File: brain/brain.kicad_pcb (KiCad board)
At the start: 2 copper layers, 48.5 x 56 mm, 7 parts, among them J0 BAR0, J1 BAR1, J2 I2C, J5 XTRA, SW1 RESET, U1 Elite-C

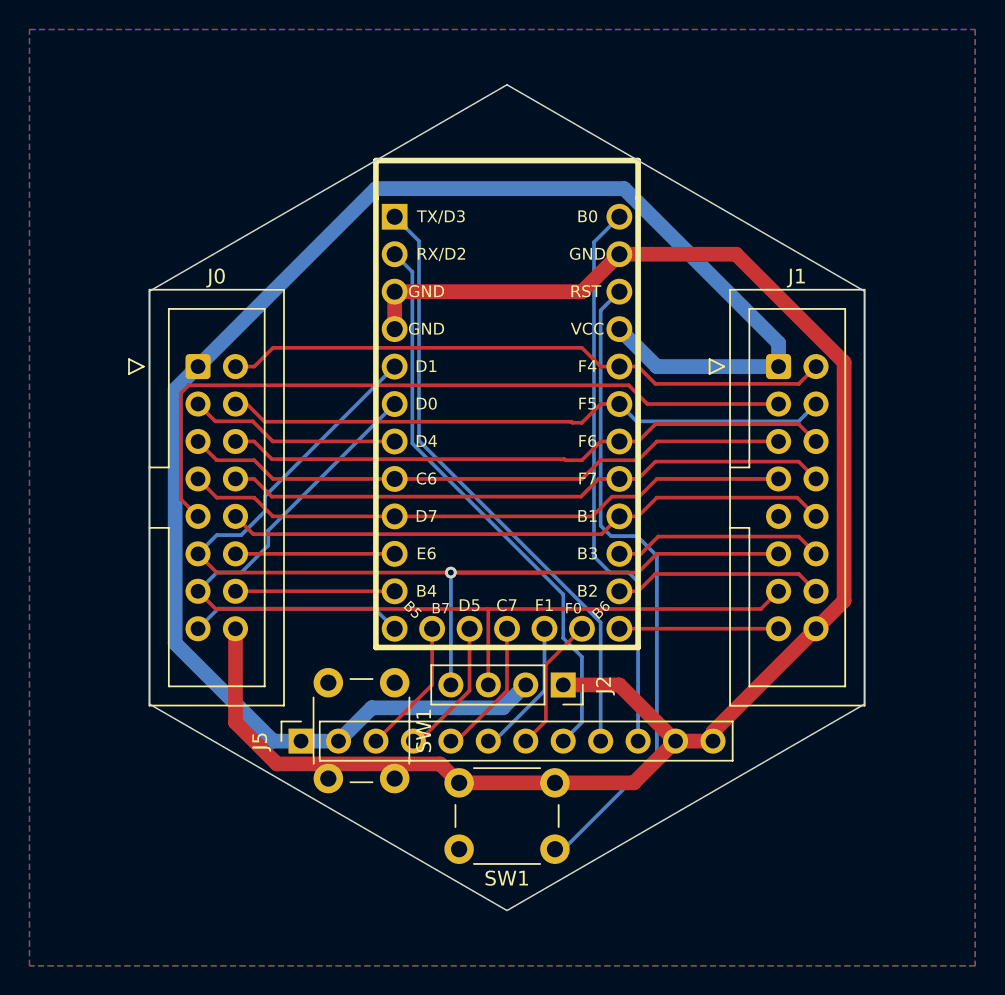
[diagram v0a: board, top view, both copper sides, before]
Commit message: Use interrupt-enabled pins for encoder0 and int1
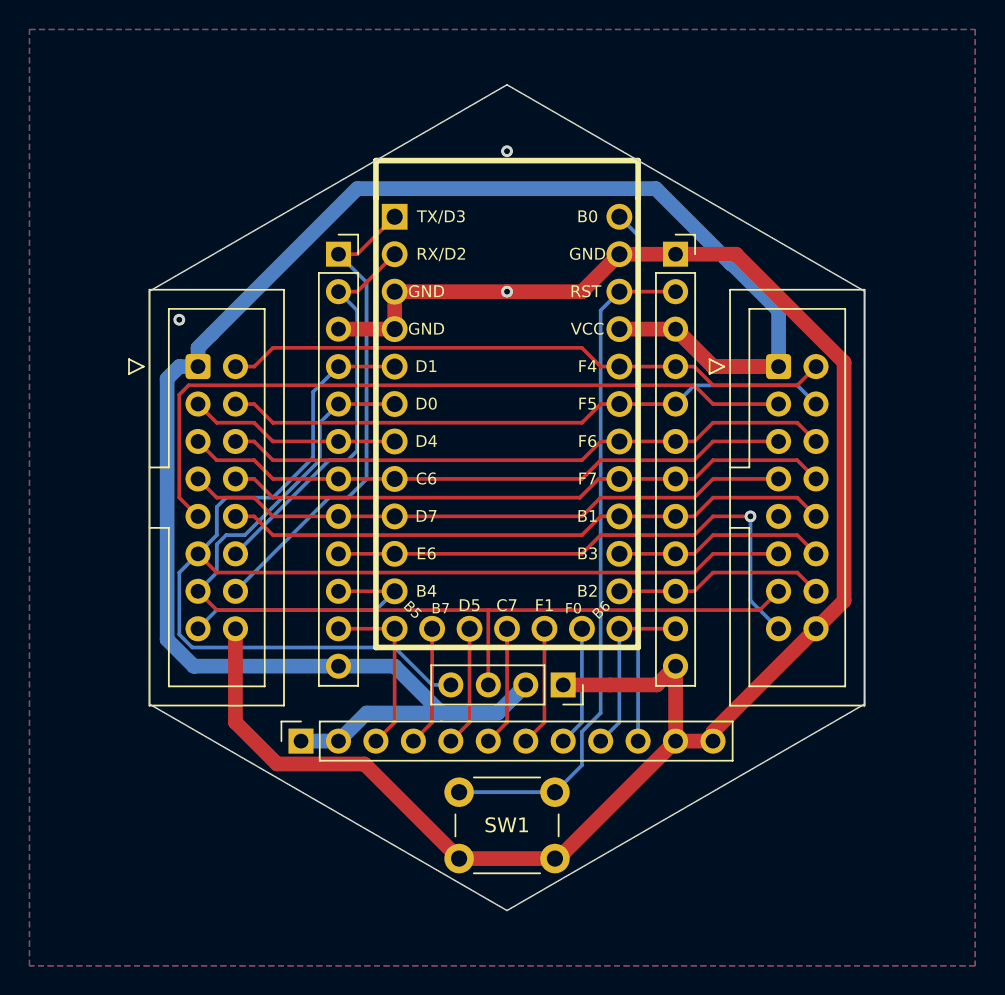
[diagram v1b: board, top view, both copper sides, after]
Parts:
- removed the SW1 at (170.2, 114.2)
- added J3: SIDE0, Connector_PinSocket_2.54mm:PinSocket_1x12_P2.54mm_Vertical, F.Cu at (166.4, 85.1)
- added J4: SIDE1, Connector_PinSocket_2.54mm:PinSocket_1x12_P2.54mm_Vertical, F.Cu at (189.2, 85.1)
- moved SW1 7.56 mm to (174.6, 121.6), turned to 0 degrees
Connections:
- J5 pad 3: /B7 -> /B5
- J5 pad 4: /D5 -> /B7
- J5 pad 5: /C7 -> /D5
- J5 pad 6: /F1 -> /C7
- J5 pad 7: /F0 -> /F1
- J5 pad 8: /RX -> /F0
- J5 pad 9: /TX -> /B6
- U1 pad 1: /TX -> /ENC0_B
- U1 pad 10: /ENC0_A -> /INT1
- U1 pad 11: /ENC0_B -> /INT0
- U1 pad 12: /INT0 -> /B5
- U1 pad 13: /INT1 -> /B6
- U1 pad 2: /RX -> /ENC0_A
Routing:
- net /TX: track 41.3 -> 0.00 mm
- net /RX: track 38.8 -> 0.00 mm
- net /INT1: track 10.8 -> 37.4 mm, vias 0 -> 1
- net VCC: track 109.7 -> 134.3 mm
- net /ENC0_B: track 10.8 -> 32.9 mm
- net /ENC0_A: track 10.8 -> 27.3 mm
- net /SDA: track 73.6 -> 88.6 mm, vias 1 -> 0
- net /B5: track 0.00 -> 12.0 mm
- net /B6: track 0.00 -> 12.0 mm
- net GND: track 117.3 -> 129.2 mm, vias 0 -> 3
- net /INT0: track 14.5 -> 18.2 mm
- net /RB0: track 38.3 -> 36.1 mm
- net /SCL: track 64.7 -> 66.7 mm
- net /RST: track 44.4 -> 46.1 mm
- net /F0: track 9.20 -> 8.14 mm
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- added copper zone on B.Cu, net GND
- removed copper zone on B.Cu, net VCC

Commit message: Brain: Add mounting holes and silkscreen labels
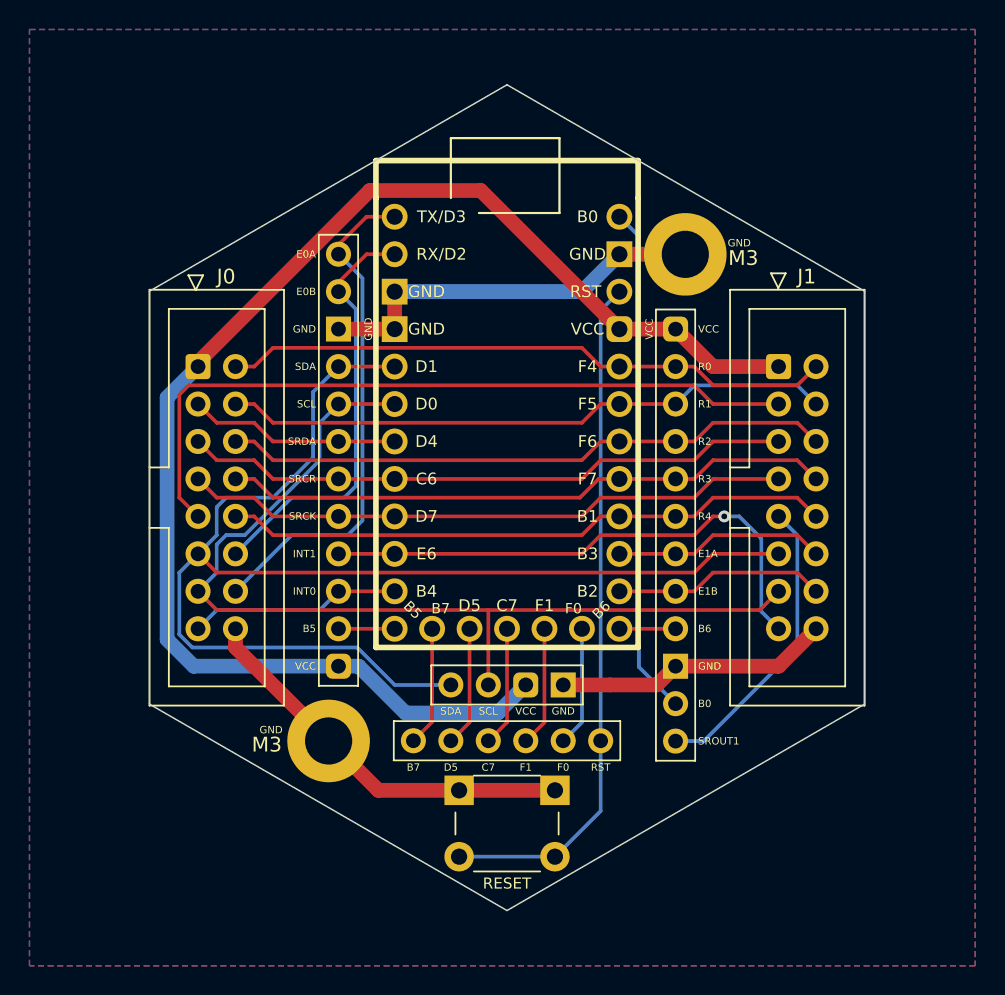
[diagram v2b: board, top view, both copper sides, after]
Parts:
- added H1: M3, MountingHole:MountingHole_3.2mm_M3_DIN965_Pad, F.Cu at (189.9, 85.1)
- added H2: M3, MountingHole:MountingHole_3.2mm_M3_DIN965_Pad, F.Cu at (165.7, 118.1)
- J5: footprint Connector_PinSocket_2.54mm:PinSocket_1x12_P2.54mm_Vertical -> Connector_PinSocket_2.54mm:PinSocket_1x06_P2.54mm_Vertical
- moved SW1 7.83 mm to (181.1, 125.9), turned to 180 degrees
- moved J5 7.62 mm to (171.4, 118.1)
- moved J4 5.08 mm to (189.2, 90.2)
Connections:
- J4 pad 1: GND -> VCC
- J4 pad 10: /ENC1_B -> GND
- J4 pad 11: /B6 -> /RB0
- J4 pad 12: GND -> /SROUT1
- J4 pad 2: /RST -> /ROW0
- J4 pad 3: VCC -> /ROW1
- J4 pad 4: /ROW0 -> /ROW2
- J4 pad 5: /ROW1 -> /ROW3
- J4 pad 6: /ROW2 -> /ROW4
- J4 pad 7: /ROW3 -> /ENC1_A
- J4 pad 8: /ROW4 -> /ENC1_B
- J4 pad 9: /ENC1_A -> /B6
- J5 pad 1: VCC -> /B7
- J5 pad 2: VCC -> /D5
- J5 pad 3: /B5 -> /C7
- J5 pad 4: /B7 -> /F1
- J5 pad 5: /D5 -> /F0
- J5 pad 6: /C7 -> /RST
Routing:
- net GND: track 129.2 -> 72.8 mm, vias 3 -> 0
- net VCC: track 134.3 -> 96.0 mm
- net /SROUT1: track 0.00 -> 20.3 mm
- net /B5: track 12.0 -> 3.81 mm
- net /B6: track 12.0 -> 3.81 mm
- net /INT0: track 18.2 -> 14.4 mm
- net /ENC0_A: track 27.3 -> 29.0 mm
- net /ENC0_B: track 32.9 -> 34.6 mm
- net /RB0: track 36.1 -> 34.6 mm
- net /RST: track 46.1 -> 46.6 mm
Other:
- board text added: "B0"
- board text added: "B5"
- board text added: "B6"
- board text added: "B7"
- board text added: "C7"
- board text added: "D5"
- board text added: "E0A"
- board text added: "E0B"
- board text added: "E1A"
- board text added: "E1B"
- board text added: "F0"
- board text added: "F1"
- board text added: "GND"
- board text added: "INT0"
- board text added: "INT1"
- board text added: "R0"
- board text added: "R1"
- board text added: "R2"
- board text added: "R3"
- board text added: "R4"
- board text added: "RESET"
- board text added: "RST"
- board text added: "SCL"
- board text added: "SDA"
- board text added: "SQUEEZEBRAIN v1"
- board text added: "SR CLK"
- board text added: "SR CLR"
- board text added: "SR DA"
- board text added: "SR OUT 0"
- board text added: "SR OUT 1"
- board text added: "SRCK"
- board text added: "SRCLK"
- board text added: "SRCLR"
- board text added: "SRCR"
- board text added: "SRDA"
- board text added: "SROUT1"
- board text added: "VCC"
- board text added: "github.com/encukou/squeezebar"

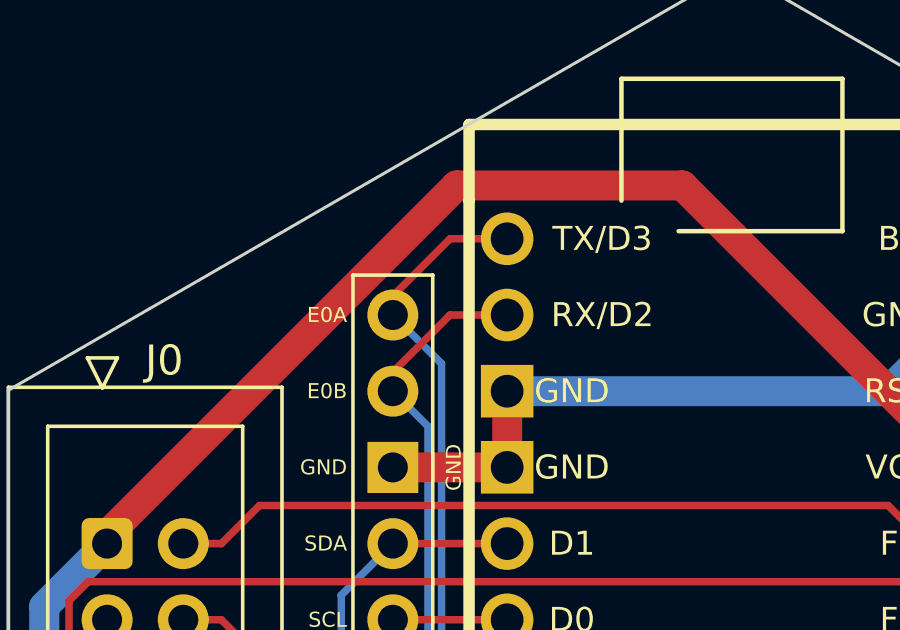
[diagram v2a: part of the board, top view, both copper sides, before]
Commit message: Add SqueezeBarrel
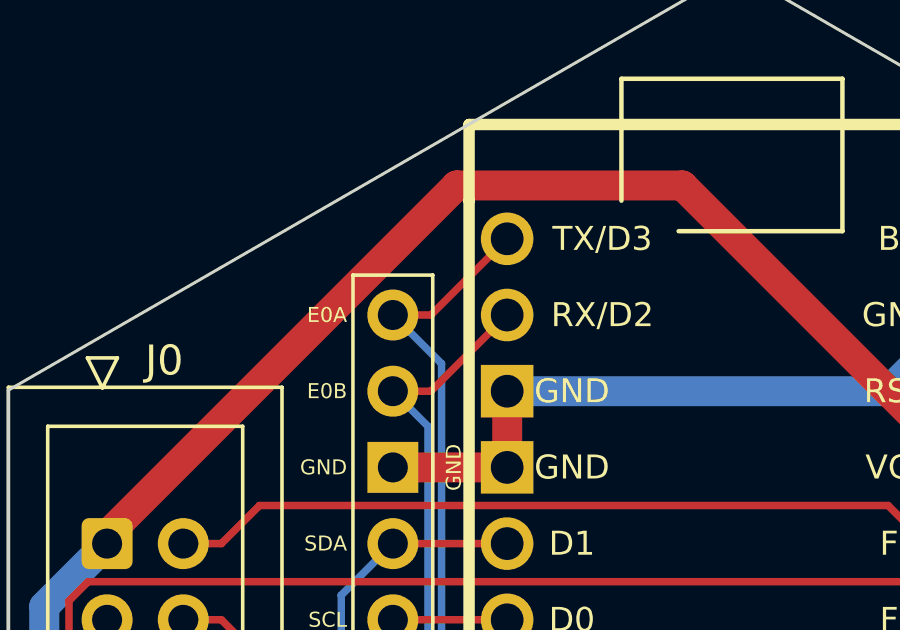
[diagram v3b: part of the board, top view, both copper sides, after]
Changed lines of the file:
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@@
   (segment (start 156.21 93.98) (end 190.5 93.98) (width 0.25) (layer "F.Cu") (net 13))
   (segment (start 155.575 94.615) (end 156.21 93.98) (width 0.25) (layer "F.Cu") (net 13))
-  (segment (start 168.275 85.09) (end 170.18 85.09) (width 0.25) (layer "F.Cu") (net 14))
-  (segment (start 166.37 87.63) (end 166.37 86.995) (width 0.25) (layer "F.Cu") (net 14))
-  (segment (start 166.37 86.995) (end 168.275 85.09) (width 0.25) (layer "F.Cu") (net 14))
+  (segment (start 167.64 87.63) (end 170.18 85.09) (width 0.25) (layer "F.Cu") (net 14))
+  (segment (start 166.37 87.63) (end 167.64 87.63) (width 0.25) (layer "F.Cu") (net 14))
   (segment (start 166.761701 101.6) (end 167.545 100.816701) (width 0.25) (layer "B.Cu") (net 14))
   (segment (start 167.545 88.805) (end 166.37 87.63) (width 0.25) (layer "B.Cu") (net 14))
@@
   (segment (start 167.545 100.816701) (end 167.545 88.805) (width 0.25) (layer "B.Cu") (net 14))
   (segment (start 163.196396 101.6) (end 166.761701 101.6) (width 0.25) (layer "B.Cu") (net 14))
-  (segment (start 166.37 85.09) (end 166.37 84.455) (width 0.25) (layer "F.Cu") (net 15))
-  (segment (start 166.37 84.455) (end 168.275 82.55) (width 0.25) (layer "F.Cu") (net 15))
-  (segment (start 168.275 82.55) (end 170.18 82.55) (width 0.25) (layer "F.Cu") (net 15))
+  (segment (start 170.18 82.55) (end 167.64 85.09) (width 0.25) (layer "F.Cu") (net 15))
+  (segment (start 167.64 85.09) (end 166.37 85.09) (width 0.25) (layer "F.Cu") (net 15))
   (segment (start 167.005 104.14) (end 163.195 104.14) (width 0.25) (layer "B.Cu") (net 15))
   (segment (start 167.995 86.715) (end 167.995 103.15) (width 0.25) (layer "B.Cu") (net 15))
